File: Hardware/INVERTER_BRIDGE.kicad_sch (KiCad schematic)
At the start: 105 parts, among them Q1 CSD19532Q5B, Q2 CSD19532Q5B, Q3 CSD19532Q5B, Q4 CSD19532Q5B, Q5 CSD19532Q5B, Q6 CSD19532Q5B, U12 UCC27282DRCR, U13 INA240A1PWR, U14 UCC27282DRCR, U15 INA240A1PWR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

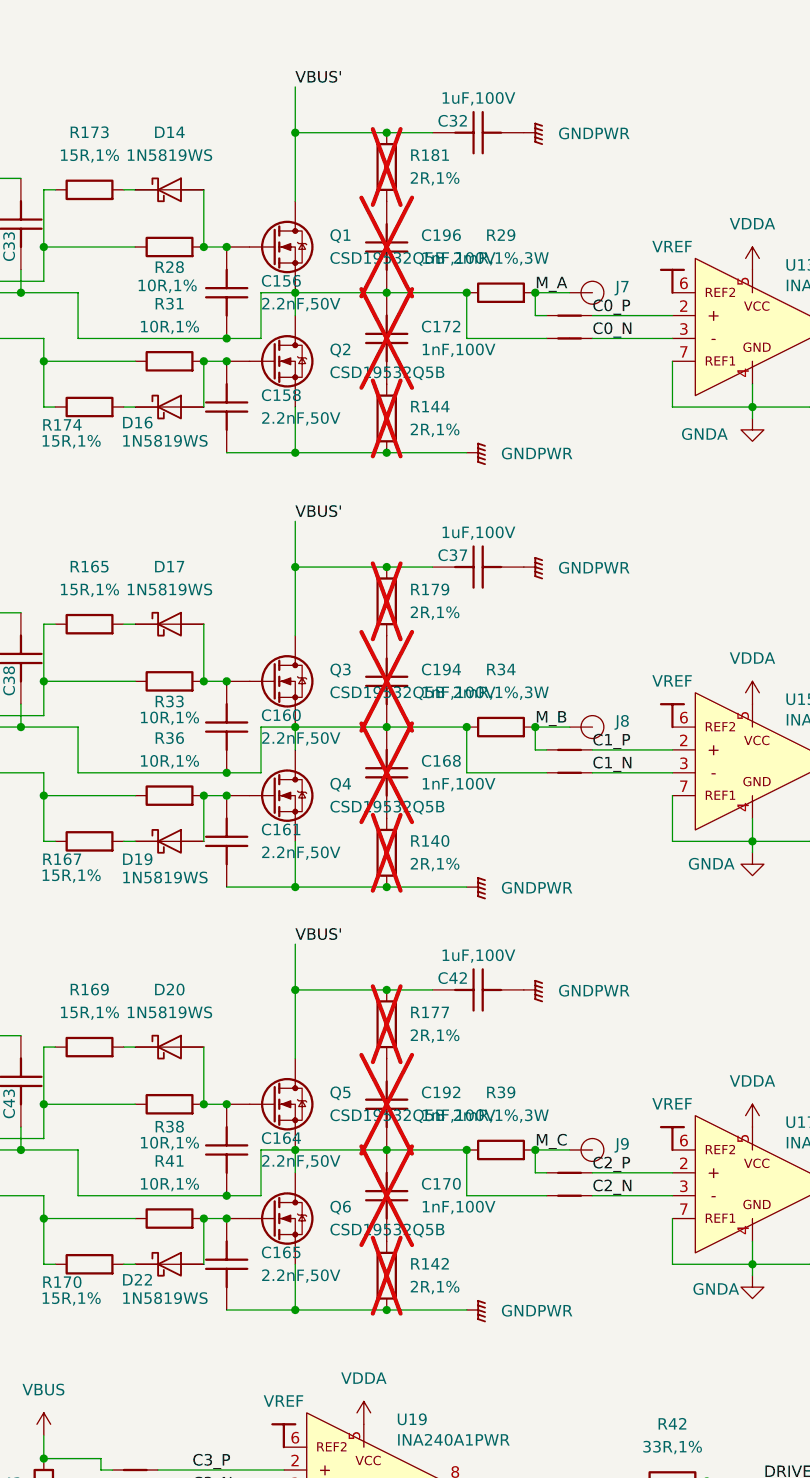
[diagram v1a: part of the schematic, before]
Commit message: 更改网口接地，更改RC吸收封装
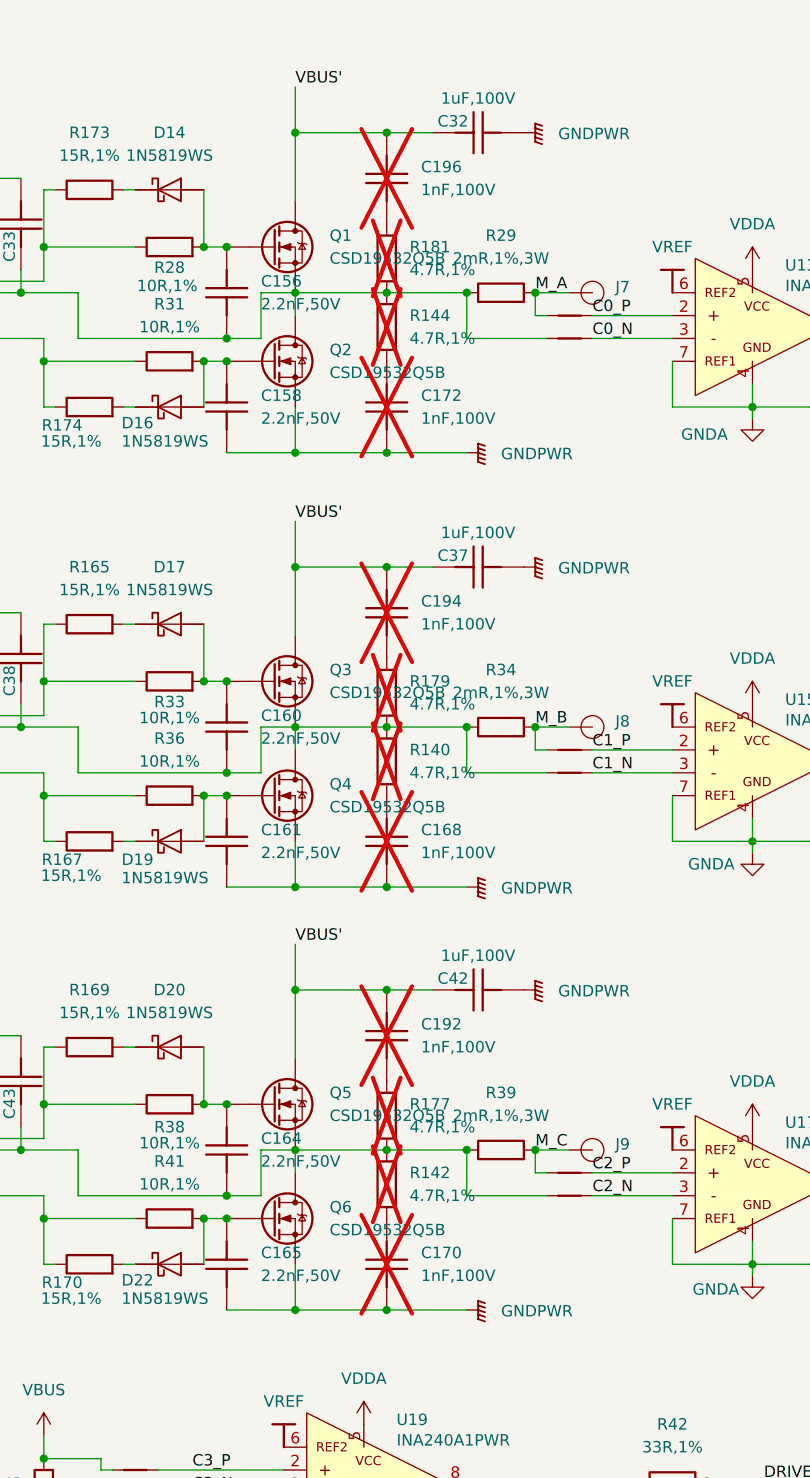
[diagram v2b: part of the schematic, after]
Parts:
- C168, C170, C172, C192, C194, C196: footprint Capacitor_SMD:C_0402_1005Metric -> Capacitor_SMD:C_0603_1608Metric; symbol HPM6280Foc:CC0402KRX7R0BB102 -> HPM6280Foc:CC0603KRX7R0BB102; 立创编号 C527013 -> C106247
- R140, R142, R144, R177, R179, R181: value 2R,1% -> 4.7R,1%; footprint Resistor_SMD:R_0402_1005Metric -> Resistor_SMD:R_0603_1608Metric; symbol HPM6280Foc:0402WGF200KTCE -> HPM6280Foc:0603WAF470KT5E; 立创编号 C270630 -> C23164
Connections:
- net GNDPWR: now also C168.2, C170.2, C172.2; no longer R140.1, R142.1, R144.1
- net VBUS': now also C192.1, C194.1, C196.1; no longer R177.2, R179.2, R181.2
- net at C156.2, C33.2, NT2.1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: now also R144.2, R181.1; no longer C172.1, C196.2
- net at R179.1: now also C160.2, C38.2, NT4.1, Q3.3 (S), Q4.1 (D), R140.2, R34.1, U14.5 (HS); no longer C194.1
- net at C164.2, C43.2, NT6.1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: now also R142.2, R177.1; no longer C170.1, C192.2
- new net: C194.2, R179.2
- new net: C196.2, R181.2
- new net: C168.1, R140.1
- new net: C192.2, R177.2
- new net: C170.1, R142.1
- new net: C172.1, R144.1
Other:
- moved on the sheet: C168, C170, C172, C192, C194, C196, R140, R142, R144, R177, R179, R181
